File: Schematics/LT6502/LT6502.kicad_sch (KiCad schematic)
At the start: 38 parts, among them U1 TC1232, U2 W65C02S6TQG-14, U3 IS62C256AL, U4 IS62C256AL, U5 SST39SF010

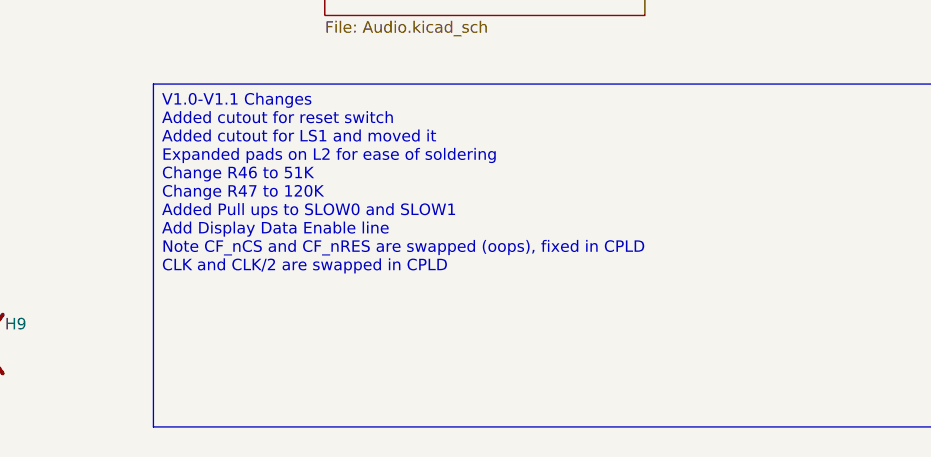
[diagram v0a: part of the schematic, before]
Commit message: Updated Schematic/PCB
Fixed battery connector polarity to save swapping wires.
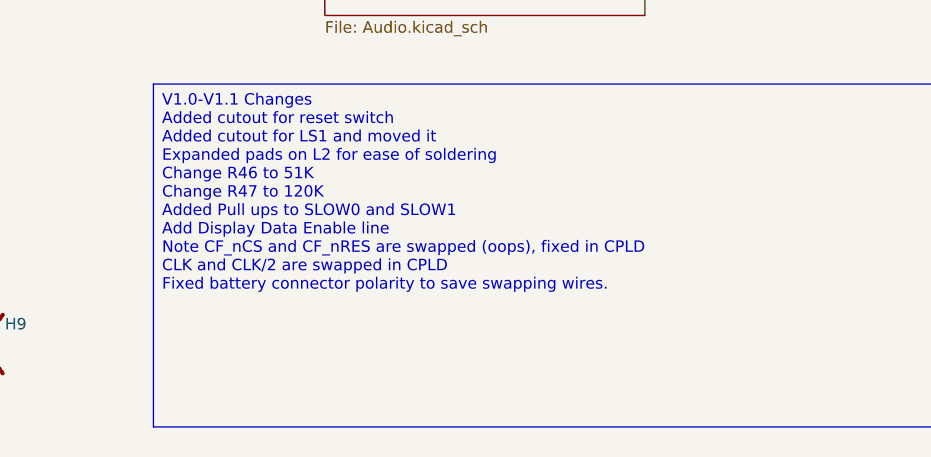
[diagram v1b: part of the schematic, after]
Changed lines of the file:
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@@
 		)
 	)
-	(text_box "V1.0-V1.1 Changes\nAdded cutout for reset switch\nAdded cutout for LS1 and moved it\nExpanded pads on L2 for ease of soldering\nChange R46 to 51K\nChange R47 to 120K\nAdded Pull ups to SLOW0 and SLOW1\nAdd Display Data Enable line\nNote CF_nCS and CF_nRES are swapped (oops), fixed in CPLD\nCLK and CLK/2 are swapped in CPLD"
+	(text_box "V1.0-V1.1 Changes\nAdded cutout for reset switch\nAdded cutout for LS1 and moved it\nExpanded pads on L2 for ease of soldering\nChange R46 to 51K\nChange R47 to 120K\nAdded Pull ups to SLOW0 and SLOW1\nAdd Display Data Enable line\nNote CF_nCS and CF_nRES are swapped (oops), fixed in CPLD\nCLK and CLK/2 are swapped in CPLD\nFixed battery connector polarity to save swapping wires."
 		(exclude_from_sim no)
 		(at 179.07 238.76 0)

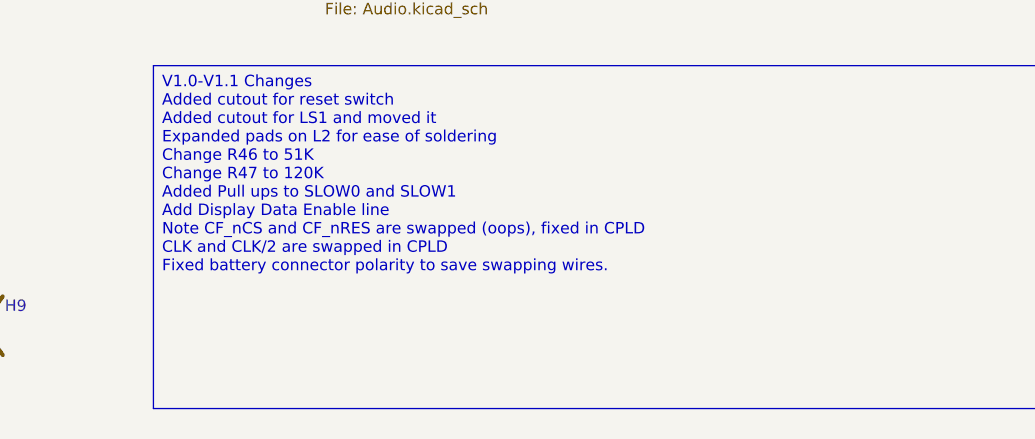
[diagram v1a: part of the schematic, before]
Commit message: Expansion Template + Main Board update
Created an expansion board template with main connector and correct PCB size
Fixed bug with Charging circuit on main board that meant it wouldn't charge when off.
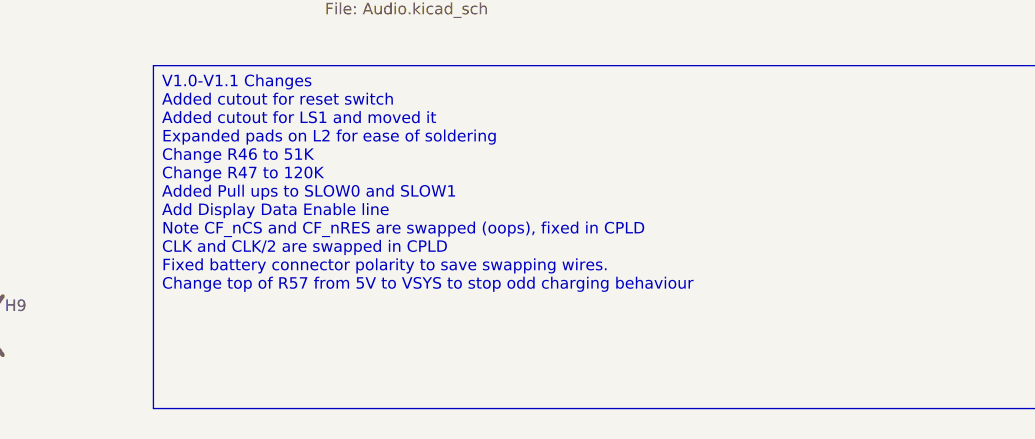
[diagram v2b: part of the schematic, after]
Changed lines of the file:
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@@
 		)
 	)
-	(text_box "V1.0-V1.1 Changes\nAdded cutout for reset switch\nAdded cutout for LS1 and moved it\nExpanded pads on L2 for ease of soldering\nChange R46 to 51K\nChange R47 to 120K\nAdded Pull ups to SLOW0 and SLOW1\nAdd Display Data Enable line\nNote CF_nCS and CF_nRES are swapped (oops), fixed in CPLD\nCLK and CLK/2 are swapped in CPLD\nFixed battery connector polarity to save swapping wires."
+	(text_box "V1.0-V1.1 Changes\nAdded cutout for reset switch\nAdded cutout for LS1 and moved it\nExpanded pads on L2 for ease of soldering\nChange R46 to 51K\nChange R47 to 120K\nAdded Pull ups to SLOW0 and SLOW1\nAdd Display Data Enable line\nNote CF_nCS and CF_nRES are swapped (oops), fixed in CPLD\nCLK and CLK/2 are swapped in CPLD\nFixed battery connector polarity to save swapping wires.\nChange top of R57 from 5V to VSYS to stop odd charging behaviour"
 		(exclude_from_sim no)
 		(at 179.07 238.76 0)

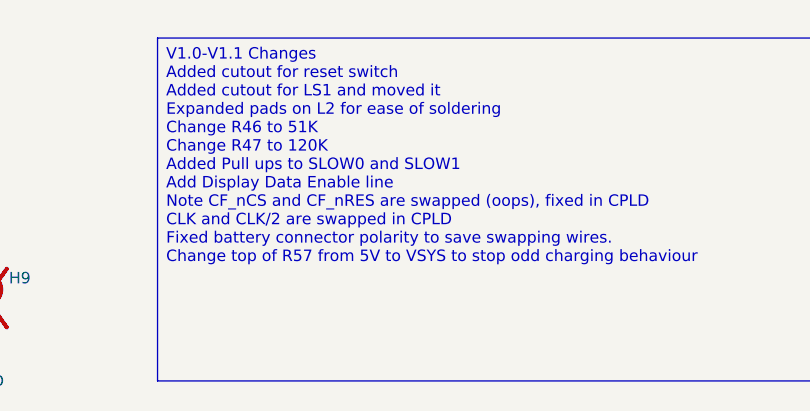
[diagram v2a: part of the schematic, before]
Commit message: LED value change, added fix for FTDI power
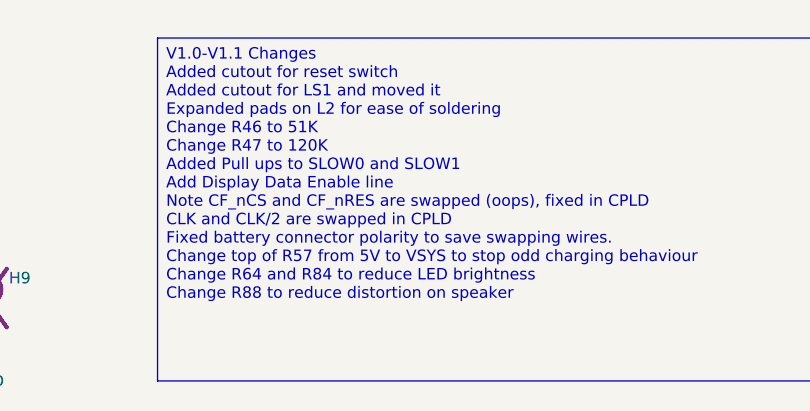
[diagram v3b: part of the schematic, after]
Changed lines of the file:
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@@
 		)
 	)
-	(text_box "V1.0-V1.1 Changes\nAdded cutout for reset switch\nAdded cutout for LS1 and moved it\nExpanded pads on L2 for ease of soldering\nChange R46 to 51K\nChange R47 to 120K\nAdded Pull ups to SLOW0 and SLOW1\nAdd Display Data Enable line\nNote CF_nCS and CF_nRES are swapped (oops), fixed in CPLD\nCLK and CLK/2 are swapped in CPLD\nFixed battery connector polarity to save swapping wires.\nChange top of R57 from 5V to VSYS to stop odd charging behaviour"
+	(text_box "V1.0-V1.1 Changes\nAdded cutout for reset switch\nAdded cutout for LS1 and moved it\nExpanded pads on L2 for ease of soldering\nChange R46 to 51K\nChange R47 to 120K\nAdded Pull ups to SLOW0 and SLOW1\nAdd Display Data Enable line\nNote CF_nCS and CF_nRES are swapped (oops), fixed in CPLD\nCLK and CLK/2 are swapped in CPLD\nFixed battery connector polarity to save swapping wires.\nChange top of R57 from 5V to VSYS to stop odd charging behaviour\nChange R64 and R84 to reduce LED brightness\nChange R88 to reduce distortion on speaker"
 		(exclude_from_sim no)
 		(at 179.07 238.76 0)

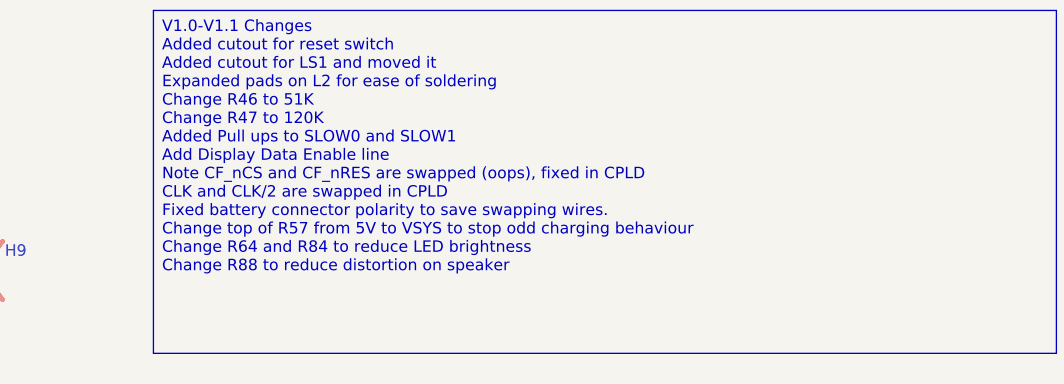
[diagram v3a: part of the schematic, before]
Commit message: PCB/Schematic edits
moved speaker hole a little
made nRES resistor for display no fit (this upsets them for some reason)
Added diodes to ensure USB Console chip is powered when nothing attached (this causes issues with booting.
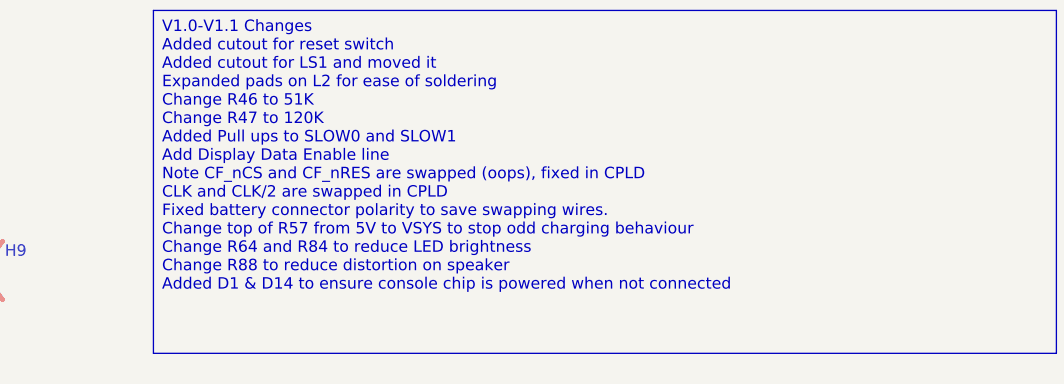
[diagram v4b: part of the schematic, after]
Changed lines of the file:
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@@
 		)
 	)
-	(text_box "V1.0-V1.1 Changes\nAdded cutout for reset switch\nAdded cutout for LS1 and moved it\nExpanded pads on L2 for ease of soldering\nChange R46 to 51K\nChange R47 to 120K\nAdded Pull ups to SLOW0 and SLOW1\nAdd Display Data Enable line\nNote CF_nCS and CF_nRES are swapped (oops), fixed in CPLD\nCLK and CLK/2 are swapped in CPLD\nFixed battery connector polarity to save swapping wires.\nChange top of R57 from 5V to VSYS to stop odd charging behaviour\nChange R64 and R84 to reduce LED brightness\nChange R88 to reduce distortion on speaker"
+	(text_box "V1.0-V1.1 Changes\nAdded cutout for reset switch\nAdded cutout for LS1 and moved it\nExpanded pads on L2 for ease of soldering\nChange R46 to 51K\nChange R47 to 120K\nAdded Pull ups to SLOW0 and SLOW1\nAdd Display Data Enable line\nNote CF_nCS and CF_nRES are swapped (oops), fixed in CPLD\nCLK and CLK/2 are swapped in CPLD\nFixed battery connector polarity to save swapping wires.\nChange top of R57 from 5V to VSYS to stop odd charging behaviour\nChange R64 and R84 to reduce LED brightness\nChange R88 to reduce distortion on speaker\nAdded D1 & D14 to ensure console chip is powered when not connected"
 		(exclude_from_sim no)
 		(at 179.07 238.76 0)

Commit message: Updated Schematics
Added bulk capacitance with higher ESR to help with display PLL starting
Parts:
- added C59: 250uF 16V, Capacitor_SMD:CP_Elec_10x12.5, symbol Device:C_Polarized
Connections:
- net +5V: now also C59.1
- net GND: now also C59.2
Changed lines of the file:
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@@
 		)
 	)
-	(text_box "V1.0-V1.1 Changes\nAdded cutout for reset switch\nAdded cutout for LS1 and moved it\nExpanded pads on L2 for ease of soldering\nChange R46 to 51K\nChange R47 to 120K\nAdded Pull ups to SLOW0 and SLOW1\nAdd Display Data Enable line\nNote CF_nCS and CF_nRES are swapped (oops), fixed in CPLD\nCLK and CLK/2 are swapped in CPLD\nFixed battery connector polarity to save swapping wires.\nChange top of R57 from 5V to VSYS to stop odd charging behaviour\nChange R64 and R84 to reduce LED brightness\nChange R88 to reduce distortion on speaker\nAdded D1 & D14 to ensure console chip is powered when not connected"
+	(text_box "V1.0-V1.1 Changes\nAdded cutout for reset switch\nAdded cutout for LS1 and moved it\nExpanded pads on L2 for ease of soldering\nChange R46 to 51K\nChange R47 to 120K\nAdded Pull ups to SLOW0 and SLOW1\nAdd Display Data Enable line\nNote CF_nCS and CF_nRES are swapped (oops), fixed in CPLD\nCLK and CLK/2 are swapped in CPLD\nFixed battery connector polarity to save swapping wires.\nChange top of R57 from 5V to VSYS to stop odd charging behaviour\nChange R64 and R84 to reduce LED brightness\nChange R88 to reduce distortion on speaker\nAdded D1 & D14 to ensure console chip is powered when not connected\nAdded 10K pull up for nRXF on FTDI\nAdded electrolytic caps to 3.3V Display supply"
 		(exclude_from_sim no)
 		(at 179.07 238.76 0)
@@
 	)
 	(junction
+		(at 74.93 142.24)
+		(diameter 0)
+		(color 0 0 0 0)
+	)
+	(junction
 		(at 167.64 170.18)
 		(diameter 0)
@@
 	(wire
 		(pts
+			(xy 74.93 138.43) (xy 74.93 142.24)
+		)
+		(stroke
+			(width 0)
+			(type default)
+		)
+	)
+	(wire
+		(pts
 			(xy 66.04 167.64) (xy 41.91 167.64)
 		)
@@
 	(wire
 		(pts
+			(xy 90.17 142.24) (xy 90.17 148.59)
+		)
+		(stroke
+			(width 0)
+			(type default)
+		)
+	)
+	(wire
+		(pts
 			(xy 132.08 110.49) (xy 147.32 110.49)
 		)
@@
 		)
 	)
+	(wire
+		(pts
+			(xy 74.93 142.24) (xy 80.01 142.24)
+		)
+		(stroke
+			(width 0)
+			(type default)
+		)
+	)
 	(bus
 		(pts
@@
 		)
 	)
+	(wire
+		(pts
+			(xy 74.93 142.24) (xy 74.93 157.48)
+		)
+		(stroke
+			(width 0)
+			(type default)
+		)
+	)
 	(bus
 		(pts
@@
 	(wire
 		(pts
+			(xy 90.17 142.24) (xy 87.63 142.24)
+		)
+		(stroke
+			(width 0)
+			(type default)
+		)
+	)
+	(wire
+		(pts
 			(xy 111.76 67.31) (xy 92.71 67.31)
 		)
@@
 	)
 	(symbol
+		(lib_id "Device:C_Polarized")
+		(at 83.82 142.24 90)
+		(unit 1)
+		(exclude_from_sim no)
+		(in_bom yes)
+		(on_board yes)
+		(dnp no)
+		(property "Reference" "C59"
+			(at 83.82 136.906 90)
+			(effects
+				(font
+					(size 1.27 1.27)
+				)
+			)
+		)
+		(property "Value" "250uF 16V"
+			(at 83.82 138.684 90)
+			(effects
+				(font
+					(size 1.27 1.27)
+				)
+			)
+		)
+		(property "Footprint" "Capacitor_SMD:CP_Elec_10x12.5"
+			(at 87.63 141.2748 0)
+			(effects
+				(font
+					(size 1.27 1.27)
+				)
+				(hide yes)
+			)
+		)
+		(property "Datasheet" "~"
+			(at 83.82 142.24 0)
+			(effects
+				(font
+					(size 1.27 1.27)
+				)
+				(hide yes)
+			)
+		)
+		(property "Description" "Polarized capacitor"
+			(at 83.82 142.24 0)
+			(effects
+				(font
+					(size 1.27 1.27)
+				)
+				(hide yes)
+			)
+		)
+		(property "Mouser Part Number" "667-EEV-FK1V681Q"
+			(at 83.82 142.24 90)
+			(effects
+				(font
+					(size 1.27 1.27)
+				)
+				(hide yes)
+			)
+		)
+		(property "LCSC" "DNF"
+			(at 83.82 142.24 90)
+			(effects
+				(font
+					(size 1.27 1.27)
+				)
+				(hide yes)
+			)
+		)
+		(pin "1"
+		)
+		(pin "2"
+		)
+		(instances
+			(project "LT6502"
+				(path "/a2243a34-697c-4939-97f7-df548e421864"
+					(reference "C59")
+					(unit 1)
+				)
+			)
+		)
+	)
+	(symbol
 		(lib_id "Device:R")
 		(at 77.47 194.31 90)
@@
 	)
 	(symbol
+		(lib_id "power:GND")
+		(at 90.17 148.59 0)
+		(unit 1)
+		(exclude_from_sim no)
+		(in_bom yes)
+		(on_board yes)
+		(dnp no)
+		(property "Reference" "#PWR0241"
+			(at 90.17 154.94 0)
+			(effects
+				(font
+					(size 1.27 1.27)
+				)
+				(hide yes)
+			)
+		)
+		(property "Value" "GND"
+			(at 90.17 153.1525 0)
+			(effects
+				(font
+					(size 1.27 1.27)
+				)
+			)
+		)
+		(property "Footprint" ""
+			(at 90.17 148.59 0)
+			(effects
+				(font
+					(size 1.27 1.27)
+				)
+				(hide yes)
+			)
+		)
+		(property "Datasheet" ""
+			(at 90.17 148.59 0)
+			(effects
+				(font
+					(size 1.27 1.27)
+				)
+				(hide yes)
+			)
+		)
+		(property "Description" ""
+			(at 90.17 148.59 0)
+			(effects
+				(font
+					(size 1.27 1.27)
+				)
+			)
+		)
+		(pin "1"
+		)
+		(instances
+			(project "LT6502"
+				(path "/a2243a34-697c-4939-97f7-df548e421864"
+					(reference "#PWR0241")
+					(unit 1)
+				)
+			)
+		)
+	)
+	(symbol
 		(lib_id "power:+5V")
 		(at 39.37 31.75 0)
@@
 	(symbol
 		(lib_id "power:+5V")
-		(at 74.93 157.48 0)
+		(at 74.93 138.43 0)
 		(unit 1)
 		(exclude_from_sim no)
@@
 		(dnp no)
 		(property "Reference" "#PWR020"
-			(at 74.93 161.29 0)
+			(at 74.93 142.24 0)
 			(effects
 				(font
@@
 		)
 		(property "Value" "+5V"
-			(at 74.93 153.924 0)
+			(at 74.93 134.874 0)
 			(effects
 				(font
@@
 		)
 		(property "Footprint" ""
-			(at 74.93 157.48 0)
+			(at 74.93 138.43 0)
 			(effects
 				(font
@@
 		)
 		(property "Datasheet" ""
-			(at 74.93 157.48 0)
+			(at 74.93 138.43 0)
 			(effects
 				(font
@@
 		)
 		(property "Description" ""
-			(at 74.93 157.48 0)
+			(at 74.93 138.43 0)
 			(effects
 				(font
